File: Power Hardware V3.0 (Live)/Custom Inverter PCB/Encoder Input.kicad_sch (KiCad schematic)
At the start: 11 parts, among them J6 1989764, U6 OP292GSZ-REEL

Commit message: Datasheets into components
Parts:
- U6: Part Number (none) -> OP292GSZ-REEL
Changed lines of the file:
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@@
 			)
 		)
-		(property "Datasheet" "OP292GSZ-REEL"
+		(property "Datasheet" "https://www.analog.com/media/en/technical-documentation/data-sheets/OP292_492.pdf"
 			(at 128.27 67.31 0)
 			(effects
@@
 			)
 		)
-		(property "Description" ""
+		(property "Description" "IC OPAMP GP 2 CIRCUIT 8SOIC"
 			(at 128.27 67.31 0)
 			(effects
+				(font
+					(size 1.27 1.27)
+				)
+				(hide yes)
+			)
+		)
+		(property "Part Number" "OP292GSZ-REEL"
+			(at 128.27 67.31 0)
+			(effects

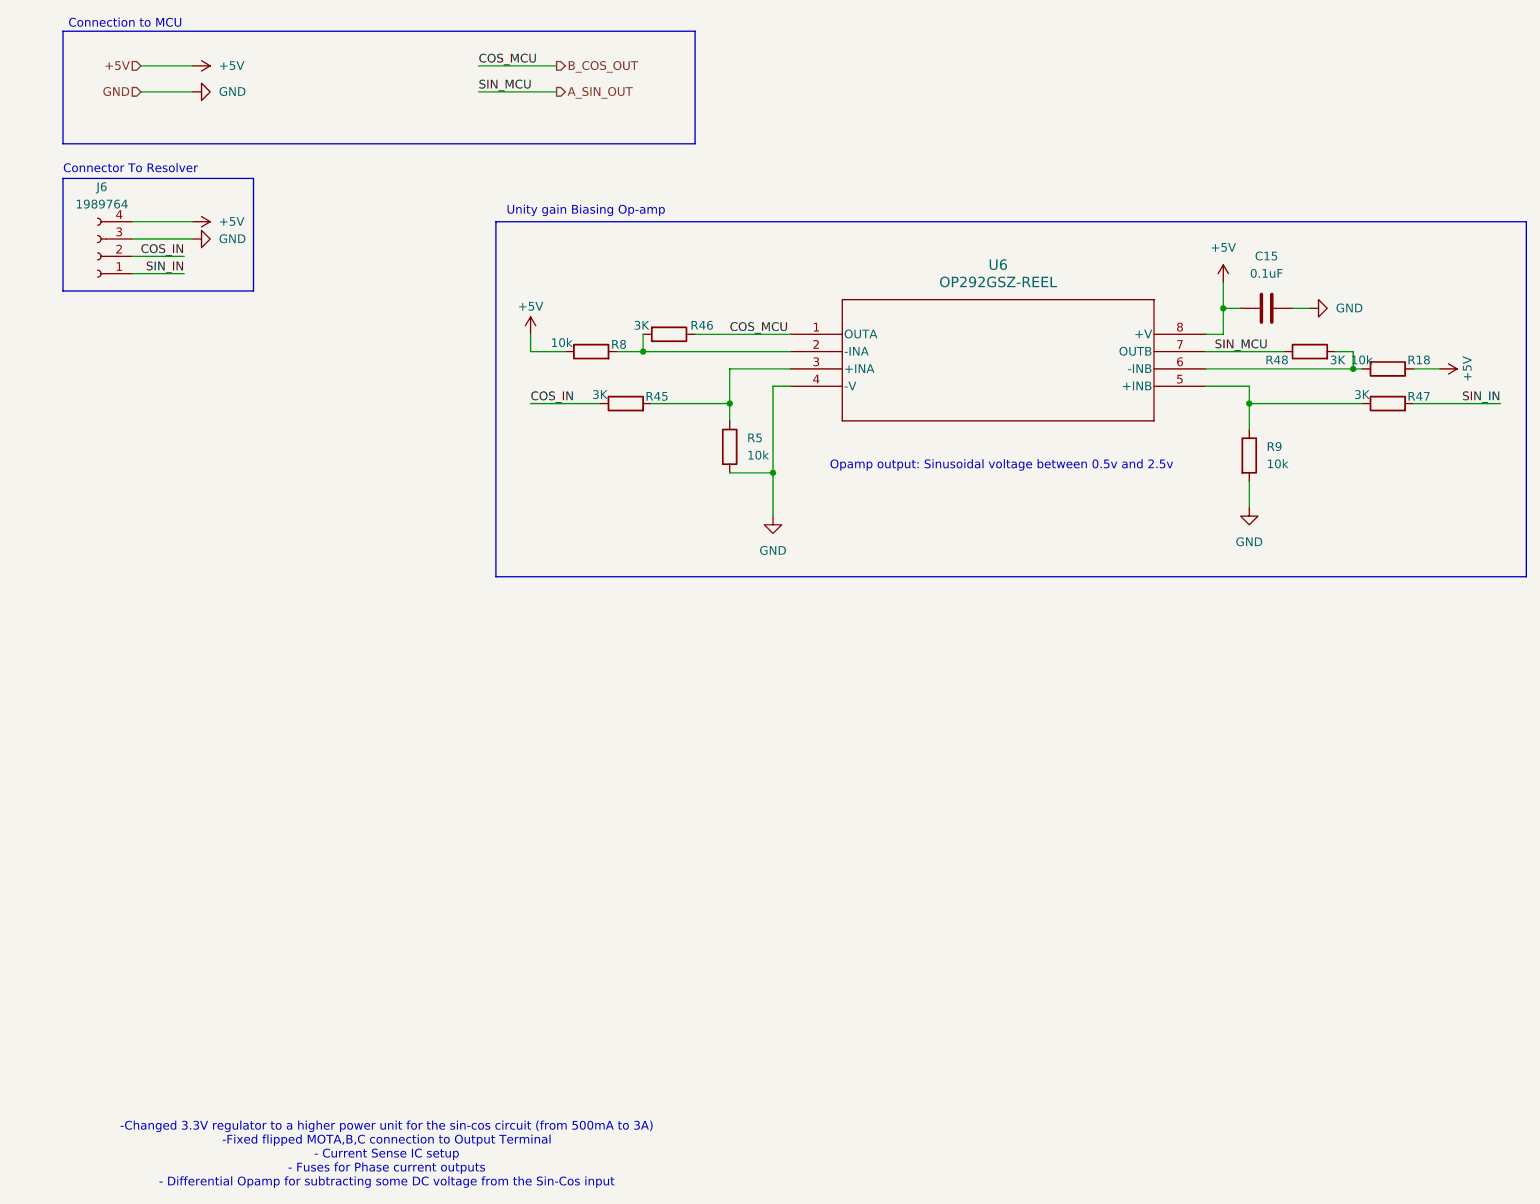
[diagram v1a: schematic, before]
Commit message: PCB V3 changes
-HV outputs and inputs changed to screw terminals for lugs
- Fuses changes to 50A
- ADC pin for temp sense along with the temp sensing circuit
- Added more pins to motor encoder term for temp sense
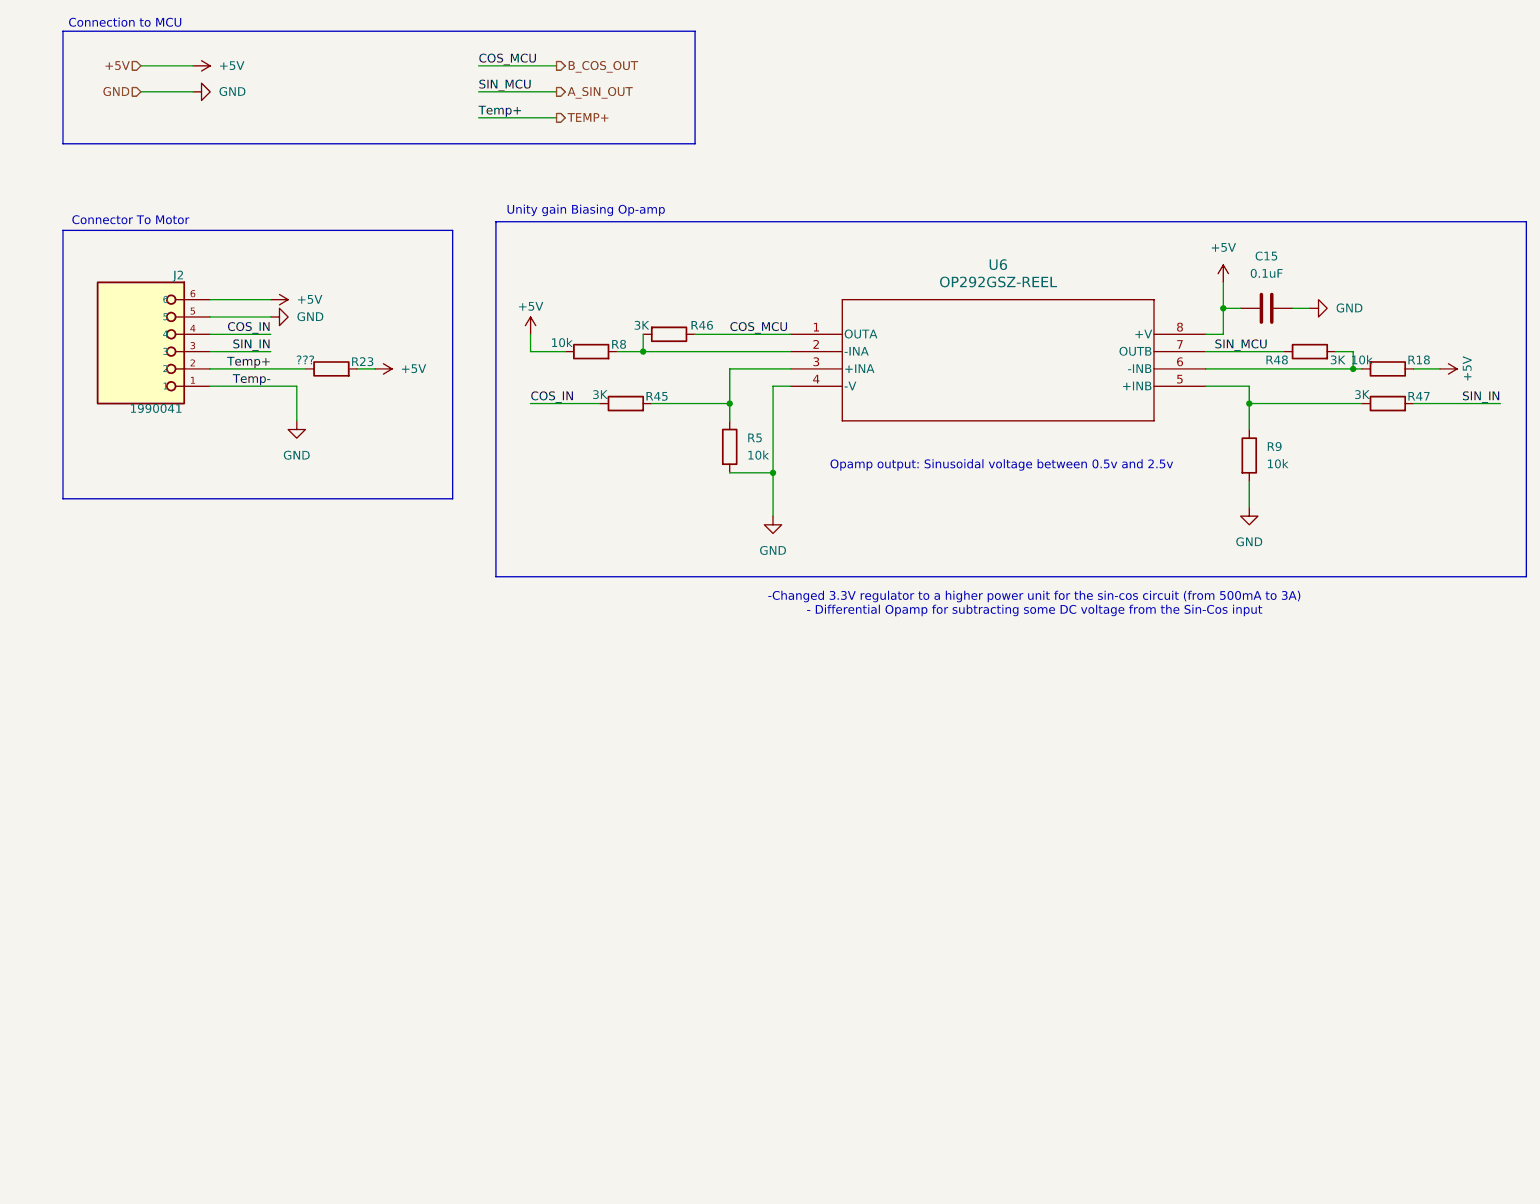
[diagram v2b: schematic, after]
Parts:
- removed J6: 1989764, PHOENIX_1989764:PHOENIX_1989764, symbol Connector:Conn_01x04_Socket
- added J2: 1990041, PHOENIX_1990041:PHOENIX_1990041, symbol PHOENIX_1990041:1990041
- R23: renamed from R45; value 3K -> ???; Part Number CRG0805F3K0 -> (none)
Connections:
- net +5V: now also R23.2, J2.6
- net COS_IN: now also J2.4
- net GND: now also J2.1, J2.5
- net SIN_IN: now also J2.3
- new net TEMP+: J2.2, R23.1
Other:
- note added: "-Changed 3.3V regulator to a higher power unit for the sin-cos circuit (from 500mA to 3A) - Differential Opamp for subtracting some DC voltage from the Sin-Cos input"
- note added: "Connector To Motor"
- note removed: "-Changed 3.3V regulator to a higher power unit for the sin-cos circuit (from 500mA to 3A) -Fixed flipped MOTA,B,C connection to Output Terminal - Current Sense IC setup - Fuses for Phase current outputs - Differential Opamp for subtracting some DC voltage from the Sin-Cos input"
- note removed: "Connector To Resolver"

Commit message: PCB layout
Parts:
- removed C15: 0.1uF, Capacitor_SMD:C_0805_2012Metric, symbol Device:C
- added C17: 0.1uF, Capacitor_SMD:C_0805_2012Metric, symbol Device:C
- added R20: 5.36k, Resistor_SMD:R_0805_2012Metric, symbol Device:R
- R22: renamed from R23; value ??? -> 3K; Part Number (none) -> CRG0805F3K0
- renumbered J2 to J6, R8 to R21, R46 to R23, R5 to R24, R9 to R25, R48 to R26, R18 to R27, R47 to R28
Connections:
- net +5V: now also C17.1, R20.2; no longer R22.2
- net GND: now also C17.2
- net TEMP+: now also R20.1; no longer R22.1

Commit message: V3 push
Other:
- note added: "- Differential Opamp for subtracting some DC voltage from the Sin-Cos input"
- note removed: "-Changed 3.3V regulator to a higher power unit for the sin-cos circuit (from 500mA to 3A) - Differential Opamp for subtracting some DC voltage from the Sin-Cos input"
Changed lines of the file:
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@@
 		)
 	)
-	(text "-Changed 3.3V regulator to a higher power unit for the sin-cos circuit (from 500mA to 3A)\n- Differential Opamp for subtracting some DC voltage from the Sin-Cos input\n"
+	(text "- Differential Opamp for subtracting some DC voltage from the Sin-Cos input\n"
 		(exclude_from_sim no)
 		(at 164.084 106.934 0)

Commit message: changes
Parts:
- R21: Part Number (none) -> ERA-6AEB103V
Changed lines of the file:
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@@
+			)
+		)
+		(property "Part Number" "ERA-6AEB103V"
+			(at 99.06 69.85 0)
+			(effects
+				(font
+					(size 1.27 1.27)
+				)
+				(hide yes)
 			)
 		)
